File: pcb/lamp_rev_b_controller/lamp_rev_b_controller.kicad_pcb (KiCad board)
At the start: 4 copper layers, 118 x 88 mm, 155 parts, among them J1 TYPE-C 3.1 MT 16P, J10 2-pin NTC header, J11 2-pin NTC header, J12 DB128H-5.08-2P-BK-S, J13 DB128H-5.08-2P-BK-S, J15 DB128H-5.08-2P-BK-S, J16 LED NTC/ID header, J17 External camera sync header, J18 SPI/FIFO camera module header, J19 Lid/cartridge/cutoff interloc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, J2 DB128H-5.08-2P-BK-S, J20 Fan PWM/tach header, J21 2x3 UART/programming header, J22 I2C expansion header, J23 Analog optical diagnostic hea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, J24 DB128H-5.08-2P high-current h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, J4 2-pin NTC header, J5 2-pin NTC header, J6 2-pin NTC header, J7 2-pin NTC header, J8 2-pin NTC header, J9 2-pin NTC header, Q1 IRLB3813PBF TO-220 12V protot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, Q2 IRLB3813PBF TO-220 12V protot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, U1 ESP32-S3-WROOM-1-N16, U10 INA180A1IDBVR gain 20 LED cur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, U2 USBLC6-2SC6, U3 Diodes AP63203WU-7 fixed 3.3V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, U4 ADS1115IDGSR, U5 CD74HC4051M, U6 TC4427ACOA/TC4427EPA, U7 CUI/Bel P7805-2000-S 5V 2A 8-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, U8 Mean Well LDD-700H 700mA CC b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, U9 SN74LVC1G08DBVR LED_EXC_PWM A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

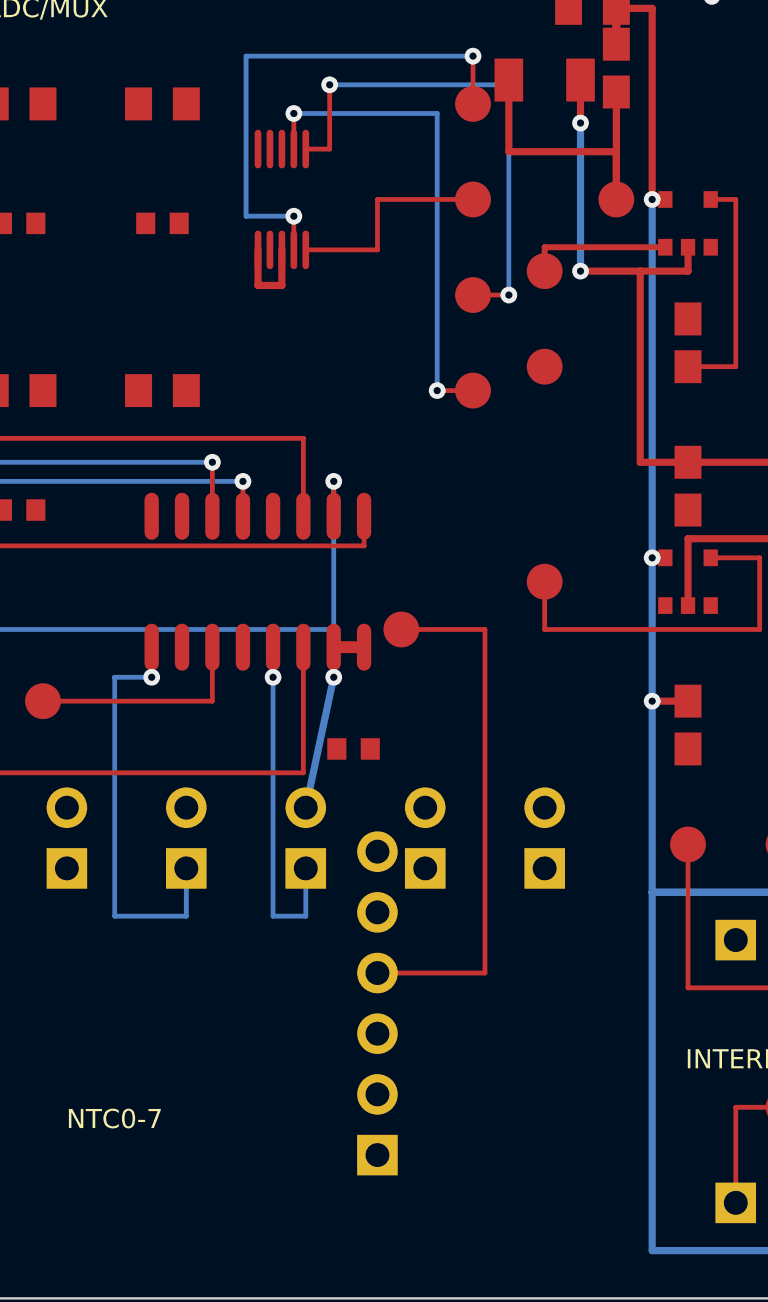
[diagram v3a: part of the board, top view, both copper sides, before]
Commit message: Reduce Rev B controller routing to 88 unconnected
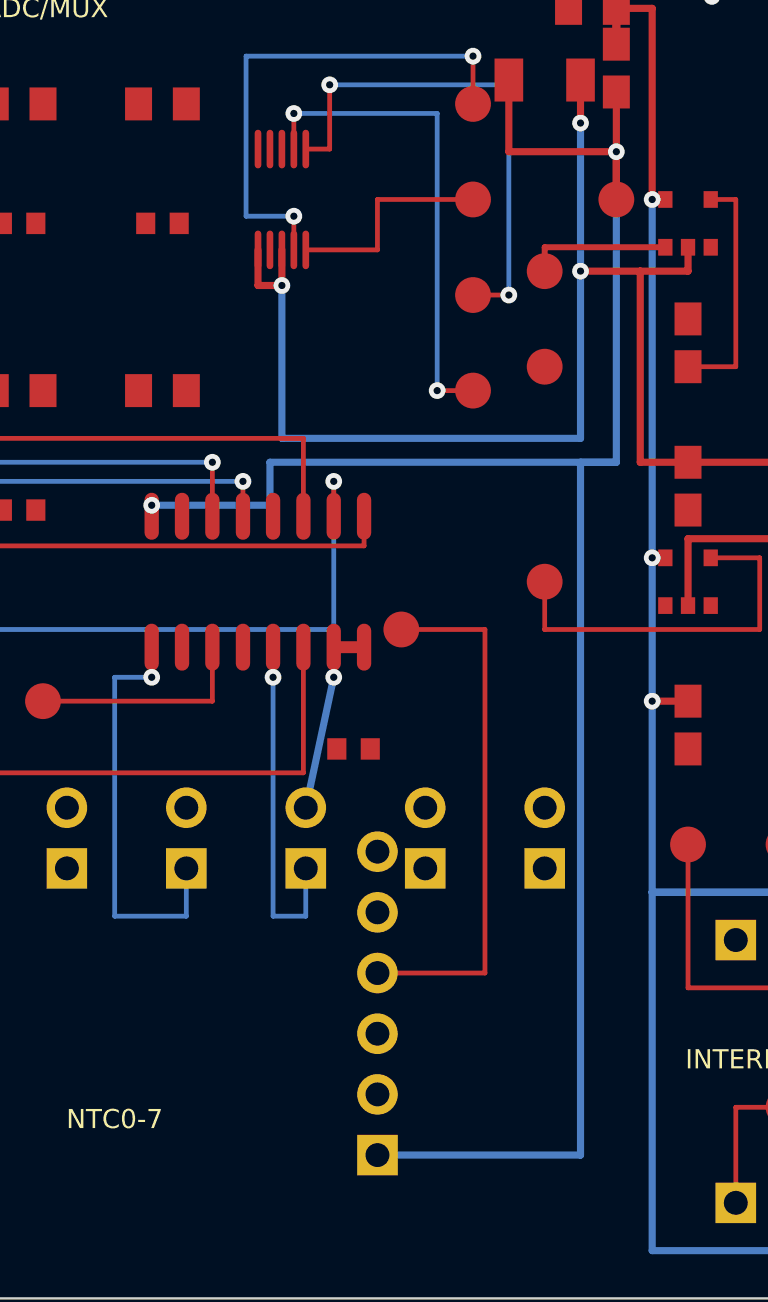
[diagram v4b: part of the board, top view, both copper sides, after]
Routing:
- net +3V3_ANA: track 14.0 -> 87.7 mm, vias 0 -> 2
- net GND: track 216.5 -> 242.4 mm, vias 8 -> 9
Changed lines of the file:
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@@
+  )
+  (via
+    (at 30 45.600)
+    (size 0.700)
+    (drill 0.300)
+    (layers "F.Cu" "B.Cu")
+    (net 1)
+  )
+  (via
+    (at 44 40)
+    (size 0.700)
+    (drill 0.300)
+    (layers "F.Cu" "B.Cu")
+    (net 12)
+  )
+  (via
+    (at 24.550 54.800)
+    (size 0.700)
+    (drill 0.300)
+    (layers "F.Cu" "B.Cu")
+    (net 12)
   )
   (via
@@
   )
   (segment
+    (start 44 40)
+    (end 44 53)
+    (width 0.300)
+    (layer "B.Cu")
+    (net 12)
+  )
+  (segment
+    (start 44 53)
+    (end 29.500 53)
+    (width 0.300)
+    (layer "B.Cu")
+    (net 12)
+  )
+  (segment
+    (start 29.500 53)
+    (end 29.500 54.800)
+    (width 0.300)
+    (layer "B.Cu")
+    (net 12)
+  )
+  (segment
+    (start 29.500 54.800)
+    (end 24.550 54.800)
+    (width 0.300)
+    (layer "B.Cu")
+    (net 12)
+  )
+  (segment
+    (start 24.550 54.800)
+    (end 24.550 55.260)
+    (width 0.300)
+    (layer "F.Cu")
+    (net 12)
+  )
+  (segment
+    (start 44 53)
+    (end 42.500 53)
+    (width 0.300)
+    (layer "B.Cu")
+    (net 12)
+  )
+  (segment
+    (start 42.500 53)
+    (end 42.500 82)
+    (width 0.300)
+    (layer "B.Cu")
+    (net 12)
+  )
+  (segment
+    (start 42.500 82)
+    (end 34 82)
+    (width 0.300)
+    (layer "B.Cu")
+    (net 12)
+  )
+  (segment
     (start 86 44)
     (end 84 44)
@@
     (net 1)
   )
+  (segment
+    (start 30 45.600)
+    (end 30 52)
+    (width 0.300)
+    (layer "B.Cu")
+    (net 1)
+  )
+  (segment
+    (start 30 52)
+    (end 42.500 52)
+    (width 0.300)
+    (layer "B.Cu")
+    (net 1)
+  )
+  (segment
+    (start 42.500 52)
+    (end 42.500 45)
+    (width 0.300)
+    (layer "B.Cu")
+    (net 1)
+  )

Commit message: Reduce Rev B controller routing to 87 unconnected
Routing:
- net ESP_GPIO0_BOOT: track 0.00 -> 28.1 mm
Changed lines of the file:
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@@
+  )
+  (segment
+    (start 54 32)
+    (end 54 34)
+    (width 0.200)
+    (layer "F.Cu")
+    (net 19)
+  )
+  (segment
+    (start 54 34)
+    (end 70.800 34)
+    (width 0.200)
+    (layer "F.Cu")
+    (net 19)
+  )
+  (segment
+    (start 70.800 34)
+    (end 70.800 25.560)
+    (width 0.200)
+    (layer "F.Cu")
+    (net 19)
+  )
+  (segment
+    (start 70.800 25.560)
+    (end 69.900 25.560)
+    (width 0.200)
+    (layer "F.Cu")
+    (net 19)
   )
   (segment

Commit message: Reduce Rev B controller routing to 86 unconnected
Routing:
- net FRAME_TRIG_OUT: track 15.1 -> 76.8 mm, vias 0 -> 2
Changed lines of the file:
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@@
+  )
+  (via
+    (at 66.720 32.500)
+    (size 0.700)
+    (drill 0.300)
+    (layers "F.Cu" "B.Cu")
+    (net 60)
+  )
+  (via
+    (at 47 67)
+    (size 0.700)
+    (drill 0.300)
+    (layers "F.Cu" "B.Cu")
+    (net 60)
   )
   (via
@@
     (width 0.200)
     (layer "F.Cu")
+    (net 60)
+  )
+  (segment
+    (start 66.720 26.950)
+    (end 66.720 32.500)
+    (width 0.200)
+    (layer "F.Cu")
+    (net 60)
+  )
+  (segment
+    (start 66.720 32.500)
+    (end 52 32.500)
+    (width 0.200)
+    (layer "B.Cu")
+    (net 60)
+  )
+  (segment
+    (start 52 32.500)
+    (end 52 66)
+    (width 0.200)
+    (layer "B.Cu")
+    (net 60)
+  )
+  (segment
+    (start 52 66)
+    (end 47 66)
+    (width 0.200)
+    (layer "B.Cu")
+    (net 60)
+  )
+  (segment
+    (start 47 66)
+    (end 47 67)
+    (width 0.200)
+    (layer "B.Cu")
+    (net 60)
+  )
+  (segment
+    (start 47 67)
+    (end 47 69)
+    (width 0.200)
+    (layer "F.Cu")

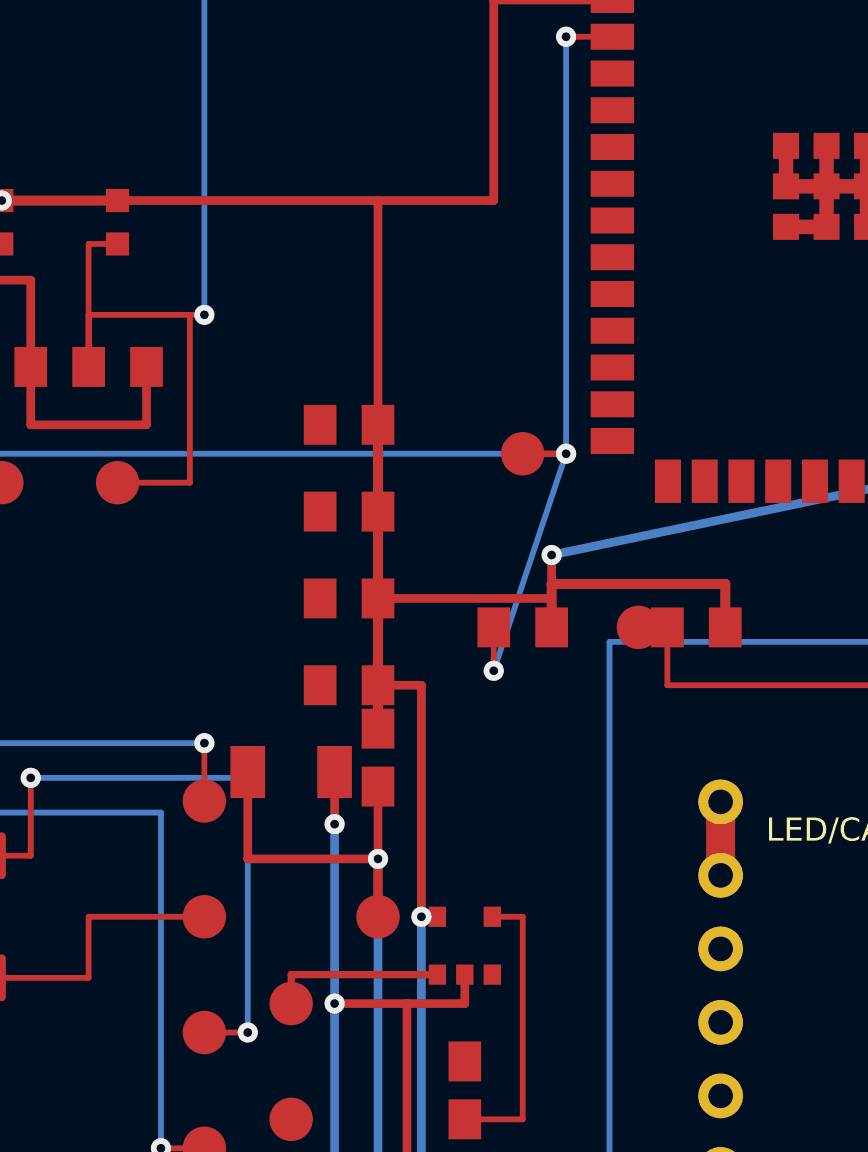
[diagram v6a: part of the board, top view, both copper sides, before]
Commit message: Reduce Rev B controller routing to 85 unconnected
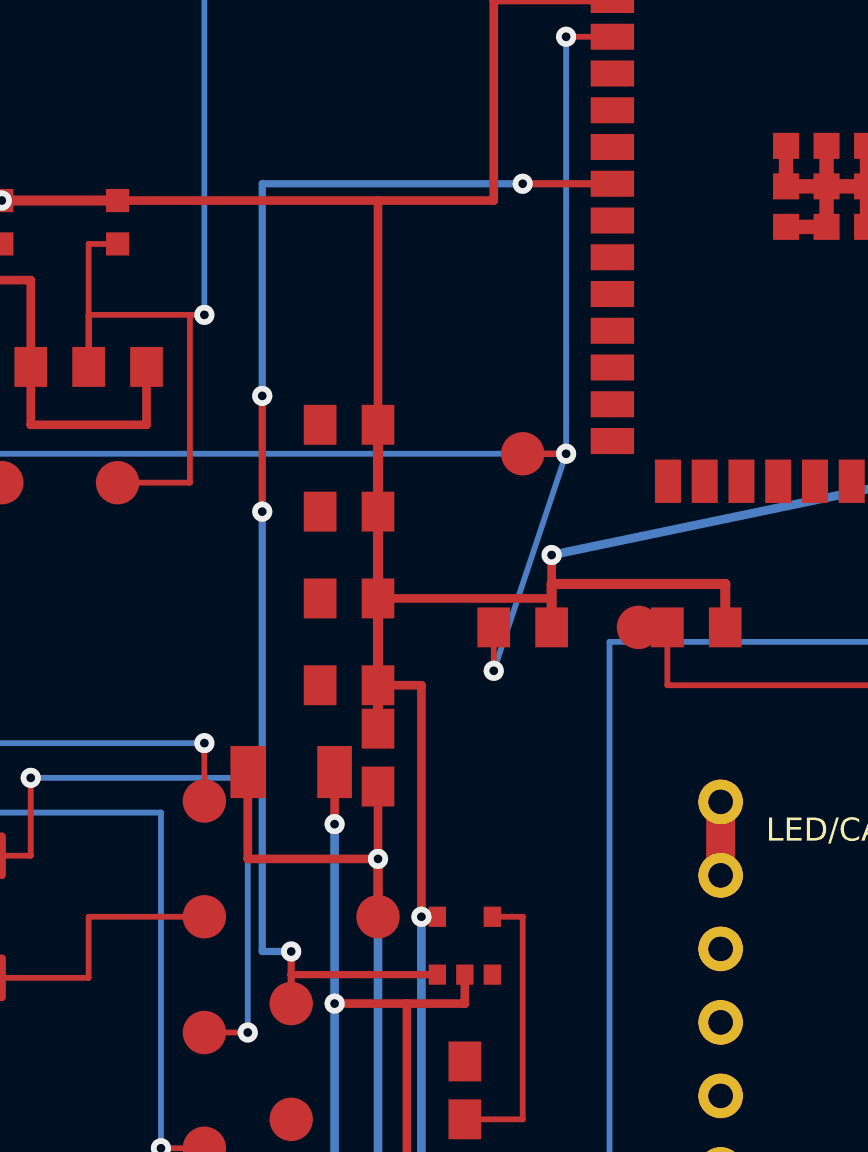
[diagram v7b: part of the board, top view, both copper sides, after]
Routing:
- net LED_EXC_PWM: track 6.05 -> 46.5 mm, vias 0 -> 4
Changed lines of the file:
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@@
+  )
+  (via
+    (at 49 16.670)
+    (size 0.700)
+    (drill 0.300)
+    (layers "F.Cu" "B.Cu")
+    (net 49)
+  )
+  (via
+    (at 41 43.200)
+    (size 0.700)
+    (drill 0.300)
+    (layers "F.Cu" "B.Cu")
+    (net 49)
+  )
+  (via
+    (at 40 24)
+    (size 0.700)
+    (drill 0.300)
+    (layers "F.Cu" "B.Cu")
+    (net 49)
+  )
+  (via
+    (at 40 28)
+    (size 0.700)
+    (drill 0.300)
+    (layers "F.Cu" "B.Cu")
+    (net 49)
   )
   (via
@@
     (width 0.250)
     (layer "F.Cu")
+    (net 49)
+  )
+  (segment
+    (start 52.100 16.670)
+    (end 49 16.670)
+    (width 0.250)
+    (layer "F.Cu")
+    (net 49)
+  )
+  (segment
+    (start 49 16.670)
+    (end 40 16.670)
+    (width 0.250)
+    (layer "B.Cu")
+    (net 49)
+  )
+  (segment
+    (start 40 16.670)
+    (end 40 24)
+    (width 0.250)
+    (layer "B.Cu")
+    (net 49)
+  )
+  (segment
+    (start 40 24)
+    (end 40 28)
+    (width 0.250)
+    (layer "F.Cu")
+    (net 49)
+  )
+  (segment
+    (start 40 28)
+    (end 40 43.200)
+    (width 0.250)
+    (layer "B.Cu")
+    (net 49)
+  )
+  (segment
+    (start 40 43.200)
+    (end 41 43.200)
+    (width 0.250)
+    (layer "B.Cu")
+    (net 49)
+  )
+  (segment
+    (start 41 43.200)
+    (end 41 44)
+    (width 0.250)
+    (layer "F.Cu")

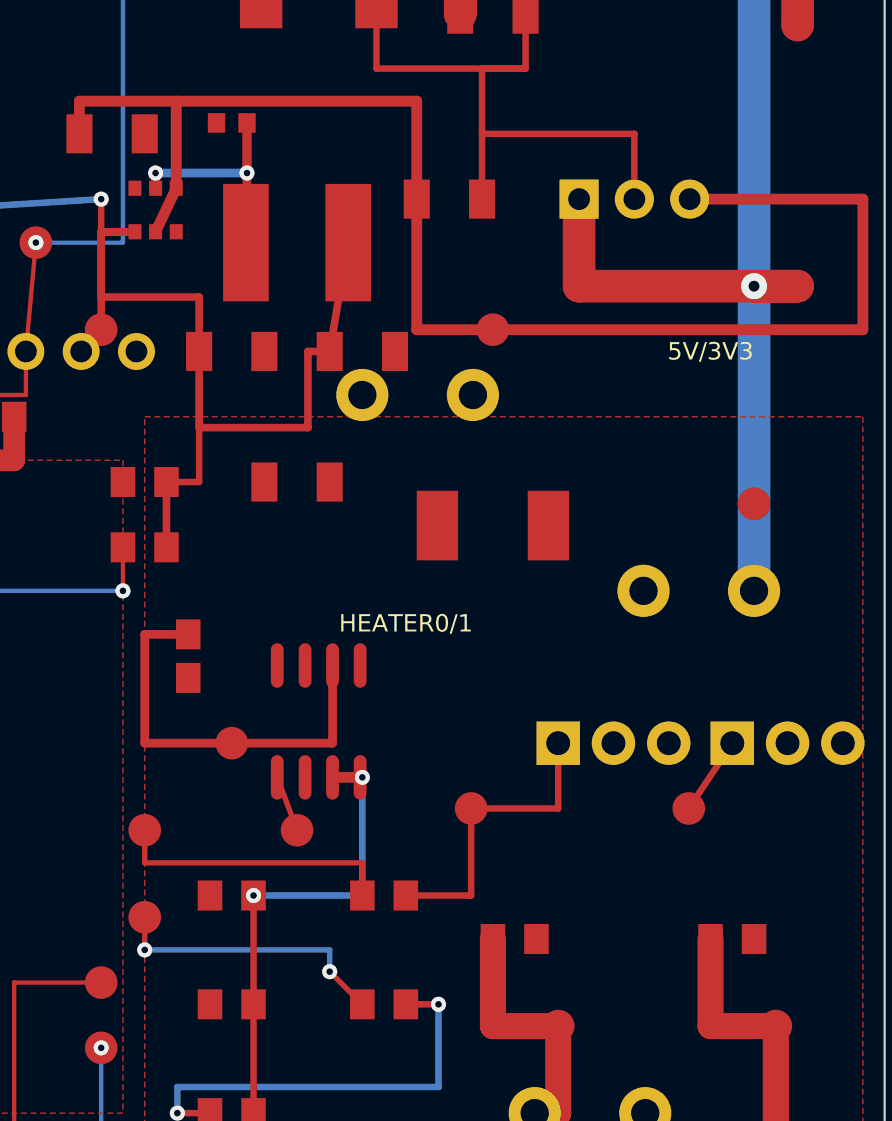
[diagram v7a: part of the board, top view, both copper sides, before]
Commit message: Reduce Rev B controller GND unconnected count to 78
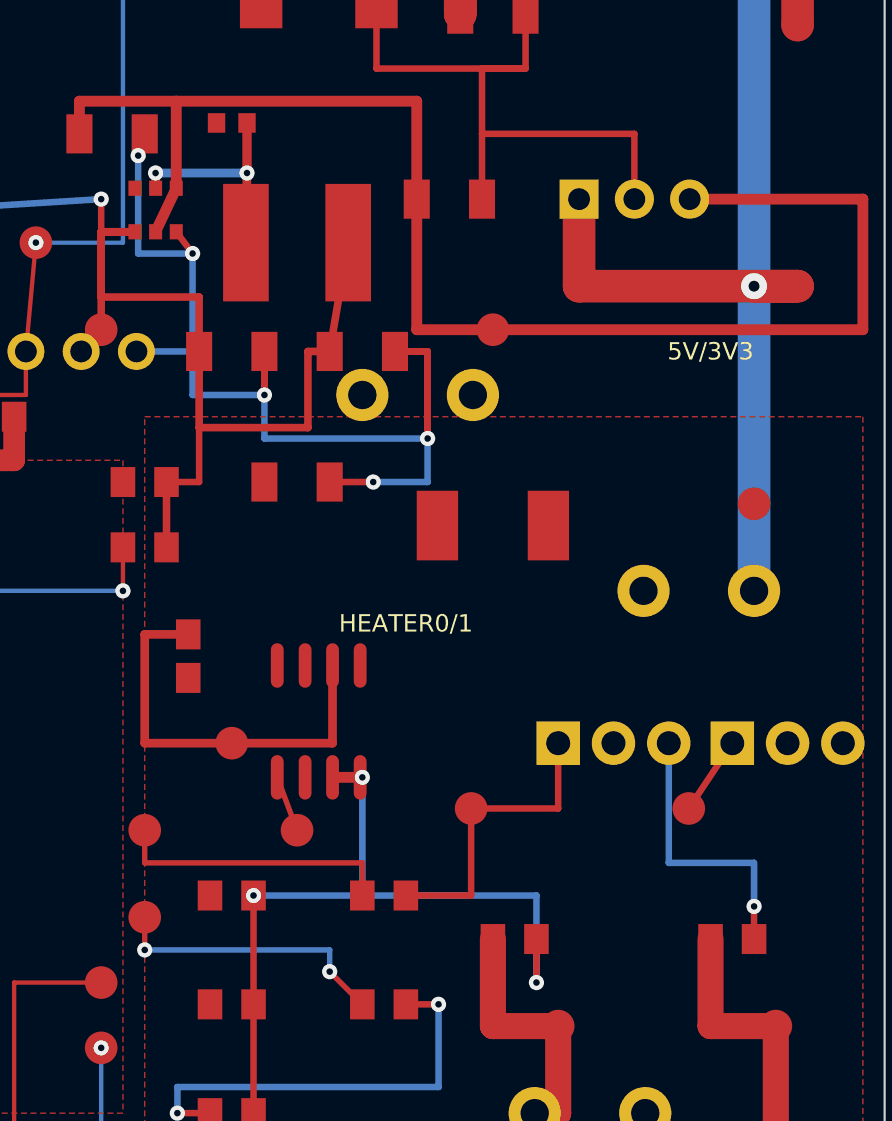
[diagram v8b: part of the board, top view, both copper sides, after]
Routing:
- net GND: track 242.4 -> 322.0 mm, vias 9 -> 16
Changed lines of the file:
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@@
     (net 77)
+  )
+  (via
+    (at 83.700 22)
+    (size 0.700)
+    (drill 0.300)
+    (layers "F.Cu" "B.Cu")
+    (net 1)
+  )
+  (via
+    (at 86.200 26.500)
+    (size 0.700)
+    (drill 0.300)
+    (layers "F.Cu" "B.Cu")
+    (net 1)
+  )
+  (via
+    (at 89.500 33)
+    (size 0.700)
+    (drill 0.300)
+    (layers "F.Cu" "B.Cu")
+    (net 1)
+  )
+  (via
+    (at 97 35)
+    (size 0.700)
+    (drill 0.300)
+    (layers "F.Cu" "B.Cu")
+    (net 1)
+  )
+  (via
+    (at 94.500 37)
+    (size 0.700)
+    (drill 0.300)
+    (layers "F.Cu" "B.Cu")
+    (net 1)
+  )
+  (via
+    (at 102 60)
+    (size 0.700)
+    (drill 0.300)
+    (layers "F.Cu" "B.Cu")
+    (net 1)
+  )
+  (via
+    (at 112 56.500)
+    (size 0.700)
+    (drill 0.300)
+    (layers "F.Cu" "B.Cu")
+    (net 1)
   )
   (segment
@@
   )
   (segment
+    (start 84 21)
+    (end 83.700 22)
+    (width 0.300)
+    (layer "F.Cu")
+    (net 1)
+  )
+  (segment
+    (start 83.700 22)
+    (end 83.700 26.500)
+    (width 0.300)
+    (layer "B.Cu")
+    (net 1)
+  )
+  (segment
+    (start 83.700 26.500)
+    (end 86.200 26.500)
+    (width 0.300)
+    (layer "B.Cu")
+    (net 1)
+  )
+  (segment
+    (start 86.200 26.500)
+    (end 85.450 25.500)
+    (width 0.300)
+    (layer "F.Cu")
+    (net 1)
+  )
+  (segment
+    (start 83.620 31)
+    (end 86.200 31)
+    (width 0.300)
+    (layer "B.Cu")
+    (net 1)
+  )
+  (segment
+    (start 86.200 31)
+    (end 86.200 26.500)
+    (width 0.300)
+    (layer "B.Cu")
+    (net 1)
+  )
+  (segment
+    (start 86.200 31)
+    (end 86.200 33)
+    (width 0.300)
+    (layer "B.Cu")
+    (net 1)
+  )
+  (segment
+    (start 86.200 33)
+    (end 89.500 33)
+    (width 0.300)
+    (layer "B.Cu")
+    (net 1)
+  )
+  (segment
+    (start 89.500 33)
+    (end 89.500 31)
+    (width 0.300)
+    (layer "F.Cu")
+    (net 1)
+  )
+  (segment
+    (start 89.500 31)
+    (end 89.500 33)
+    (width 0.300)
+    (layer "F.Cu")
+    (net 1)
+  )
+  (segment
+    (start 89.500 33)
+    (end 89.500 35)
+    (width 0.300)
+    (layer "B.Cu")
+    (net 1)
+  )
+  (segment
+    (start 89.500 35)
+    (end 97 35)
+    (width 0.300)
+    (layer "B.Cu")
+    (net 1)
+  )
+  (segment
+    (start 97 35)
+    (end 97 31)
+    (width 0.300)
+    (layer "F.Cu")
+    (net 1)
+  )
+  (segment
+    (start 97 31)
+    (end 95.500 31)
+    (width 0.300)
+    (layer "F.Cu")
+    (net 1)
+  )
+  (segment
+    (start 95.500 31)
+    (end 97 31)
+    (width 0.300)
+    (layer "F.Cu")
+    (net 1)
+  )
+  (segment
+    (start 97 31)
+    (end 97 35)
+    (width 0.300)
+    (layer "F.Cu")
+    (net 1)
+  )
+  (segment
+    (start 97 35)
+    (end 97 37)
+    (width 0.300)
+    (layer "B.Cu")
+    (net 1)
+  )
+  (segment
+    (start 97 37)
+    (end 94.500 37)
+    (width 0.300)
+    (layer "B.Cu")
+    (net 1)
+  )
+  (segment
+    (start 94.500 37)
+    (end 92.500 37)
+    (width 0.300)
+    (layer "F.Cu")
+    (net 1)
+  )
+  (segment
     (start 98.500 15.500)
     (end 98.500 11.500)
@@
     (net 1)
   )
+  (segment
+    (start 102 58)
+    (end 102 60)
+    (width 0.300)
+    (layer "F.Cu")
+    (net 1)
+  )
+  (segment
+    (start 102 60)
+    (end 102 56)
+    (width 0.300)
+    (layer "B.Cu")
+    (net 1)
+  )
+  (segment
+    (start 102 56)
+    (end 94 56)
+    (width 0.300)
+    (layer "B.Cu")
+    (net 1)
+  )
+  (segment
+    (start 108.080 49)
+    (end 108.080 54.500)
+    (width 0.300)
+    (layer "B.Cu")
+    (net 1)
+  )
+  (segment
+    (start 108.080 54.500)
+    (end 112 54.500)
+    (width 0.300)
+    (layer "B.Cu")
+    (net 1)
+  )
+  (segment
+    (start 112 54.500)
+    (end 112 56.500)
+    (width 0.300)
+    (layer "B.Cu")
+    (net 1)
+  )
+  (segment
+    (start 112 56.500)
+    (end 112 58)
+    (width 0.300)
+    (layer "F.Cu")
+    (net 1)
+  )
